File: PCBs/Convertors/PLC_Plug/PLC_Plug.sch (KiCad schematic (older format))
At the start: 23 parts, among them J1 RO21, J10 AOV2.3, J11 AOV2.4, J12 RS485-2.1, J13 RS485-2.1, J14 AO, J15 AO, J16 DO, J17 DI, J18 DI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

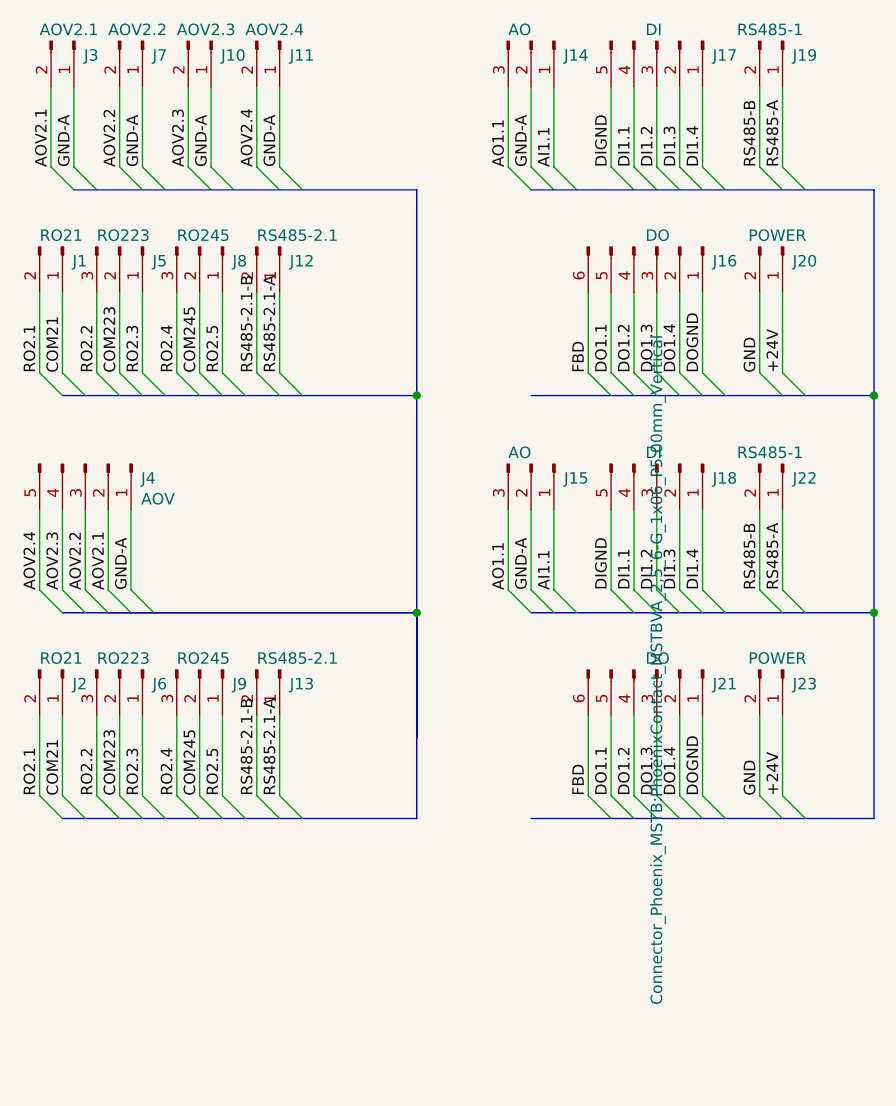
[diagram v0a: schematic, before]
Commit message: Update PLC adapter
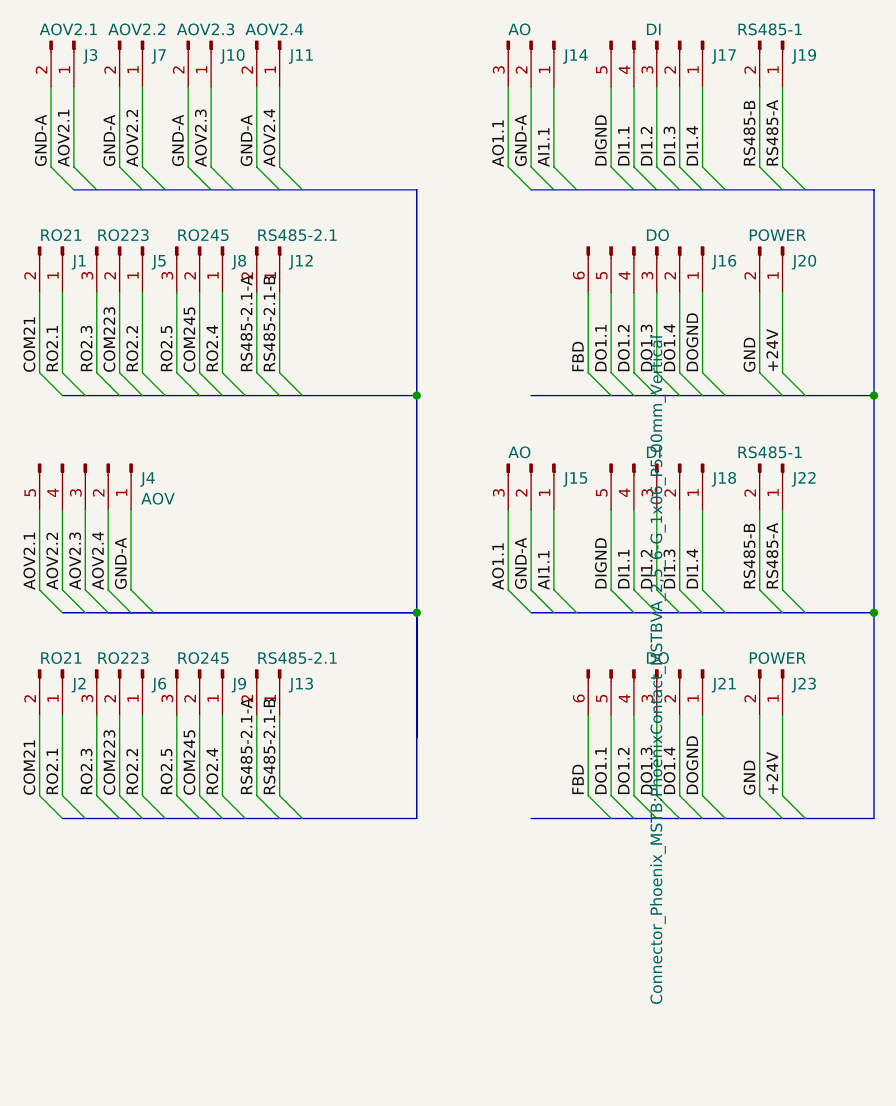
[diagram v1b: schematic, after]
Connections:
- net AOV2.1: now also J3.1 (Pin_1), J4.5 (Pin_5); no longer J3.2 (Pin_2), J4.2 (Pin_2)
- net AOV2.2: now also J4.4 (Pin_4), J7.1 (Pin_1); no longer J4.3 (Pin_3), J7.2 (Pin_2)
- net AOV2.3: now also J10.1 (Pin_1), J4.3 (Pin_3); no longer J10.2 (Pin_2), J4.4 (Pin_4)
- net AOV2.4: now also J11.1 (Pin_1), J4.2 (Pin_2); no longer J11.2 (Pin_2), J4.5 (Pin_5)
- net COM21: now also J1.2 (Pin_2), J2.2 (Pin_2); no longer J1.1 (Pin_1), J2.1 (Pin_1)
- net GND-A: now also J10.2 (Pin_2), J11.2 (Pin_2), J3.2 (Pin_2), J7.2 (Pin_2); no longer J10.1 (Pin_1), J11.1 (Pin_1), J3.1 (Pin_1), J7.1 (Pin_1)
- net RO2.1: now also J1.1 (Pin_1), J2.1 (Pin_1); no longer J1.2 (Pin_2), J2.2 (Pin_2)
- net RO2.2: now also J5.1 (Pin_1), J6.1 (Pin_1); no longer J5.3 (Pin_3), J6.3 (Pin_3)
- net RO2.3: now also J5.3 (Pin_3), J6.3 (Pin_3); no longer J5.1 (Pin_1), J6.1 (Pin_1)
- net RO2.4: now also J8.1 (Pin_1), J9.1 (Pin_1); no longer J8.3 (Pin_3), J9.3 (Pin_3)
- net RO2.5: now also J8.3 (Pin_3), J9.3 (Pin_3); no longer J8.1 (Pin_1), J9.1 (Pin_1)
- net RS485-2.1-A: now also J12.2 (Pin_2), J13.2 (Pin_2); no longer J12.1 (Pin_1), J13.1 (Pin_1)
- net RS485-2.1-B: now also J12.1 (Pin_1), J13.1 (Pin_1); no longer J12.2 (Pin_2), J13.2 (Pin_2)
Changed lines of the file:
@@
 Wire Bus Line
 	5700 4050 5700 5000
+Text Label 4200 3050 1    50   ~ 0
+AOV2.1
+Wire Wire Line
+	4100 2700 4100 3050
+Wire Wire Line
+	4200 2700 4200 3050
+Wire Wire Line
+	4400 2700 4400 3050
+Wire Wire Line
+	4500 2700 4500 3050
+Wire Wire Line
+	4700 2700 4700 3050
+Wire Wire Line
+	4800 2700 4800 3050
+Wire Wire Line
+	5000 2700 5000 3050
+Wire Wire Line
+	5100 2700 5100 3050
+Text Label 4500 3050 1    50   ~ 0
+AOV2.2
+Text Label 4800 3050 1    50   ~ 0
+AOV2.3
+Text Label 5100 3050 1    50   ~ 0
+AOV2.4
 Text Label 4100 3050 1    50   ~ 0
-AOV2.1
-Wire Wire Line
-	4100 2700 4100 3050
-Wire Wire Line
-	4200 2700 4200 3050
-Wire Wire Line
-	4400 2700 4400 3050
-Wire Wire Line
-	4500 2700 4500 3050
-Wire Wire Line
-	4700 2700 4700 3050
-Wire Wire Line
-	4800 2700 4800 3050
-Wire Wire Line
-	5000 2700 5000 3050
-Wire Wire Line
-	5100 2700 5100 3050
+GND-A
 Text Label 4400 3050 1    50   ~ 0
-AOV2.2
+GND-A
 Text Label 4700 3050 1    50   ~ 0
-AOV2.3
+GND-A
 Text Label 5000 3050 1    50   ~ 0
-AOV2.4
-Text Label 4200 3050 1    50   ~ 0
-GND-A
-Text Label 4500 3050 1    50   ~ 0
-GND-A
-Text Label 4800 3050 1    50   ~ 0
-GND-A
-Text Label 5100 3050 1    50   ~ 0
 GND-A
 Wire Wire Line
@@
 Wire Wire Line
 	4450 4900 4450 4550
+Text Label 4050 4900 1    50   ~ 0
+AOV2.1
+Text Label 4150 4900 1    50   ~ 0
+AOV2.2
+Text Label 4250 4900 1    50   ~ 0
+AOV2.3
 Text Label 4350 4900 1    50   ~ 0
-AOV2.1
-Text Label 4250 4900 1    50   ~ 0
-AOV2.2
-Text Label 4150 4900 1    50   ~ 0
-AOV2.3
-Text Label 4050 4900 1    50   ~ 0
 AOV2.4
 Text Label 4450 4900 1    50   ~ 0
 GND-A
 Connection ~ 5700 4050
+Text Label 4150 3950 1    50   ~ 0
+RO2.1
+Text Label 4500 3950 1    50   ~ 0
+RO2.2
+Text Label 4300 3950 1    50   ~ 0
+RO2.3
+Text Label 4850 3950 1    50   ~ 0
+RO2.4
+Text Label 4650 3950 1    50   ~ 0
+RO2.5
 Text Label 4050 3950 1    50   ~ 0
-RO2.1
-Text Label 4300 3950 1    50   ~ 0
-RO2.2
-Text Label 4500 3950 1    50   ~ 0
-RO2.3
-Text Label 4650 3950 1    50   ~ 0
-RO2.4
-Text Label 4850 3950 1    50   ~ 0
-RO2.5
-Text Label 4150 3950 1    50   ~ 0
 COM21
 Text Label 4400 3950 1    50   ~ 0
@@
 Wire Wire Line
 	5100 5450 5100 5800
+Text Label 4150 5800 1    50   ~ 0
+RO2.1
+Text Label 4500 5800 1    50   ~ 0
+RO2.2
+Text Label 4300 5800 1    50   ~ 0
+RO2.3
+Text Label 4850 5800 1    50   ~ 0
+RO2.4
+Text Label 4650 5800 1    50   ~ 0
+RO2.5
 Text Label 4050 5800 1    50   ~ 0
-RO2.1
-Text Label 4300 5800 1    50   ~ 0
-RO2.2
-Text Label 4500 5800 1    50   ~ 0
-RO2.3
-Text Label 4650 5800 1    50   ~ 0
-RO2.4
-Text Label 4850 5800 1    50   ~ 0
-RO2.5
-Text Label 4150 5800 1    50   ~ 0
 COM21
 Text Label 4400 5800 1    50   ~ 0
@@
 Wire Bus Line
 	5700 5000 5700 5900
+Text Label 5100 3950 1    50   ~ 0
+RS485-2.1-B
 Text Label 5000 3950 1    50   ~ 0
+RS485-2.1-A
+Text Label 5100 5800 1    50   ~ 0
 RS485-2.1-B
-Text Label 5100 3950 1    50   ~ 0
+Text Label 5000 5800 1    50   ~ 0
 RS485-2.1-A
-Text Label 5000 5800 1    50   ~ 0
-RS485-2.1-B
-Text Label 5100 5800 1    50   ~ 0
-RS485-2.1-A
-Entry Wire Line
+Entry Wire Line
